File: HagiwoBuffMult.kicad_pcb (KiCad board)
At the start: 2 copper layers, 25 x 108.3 mm, 41 parts, among them J1 IN1, J10 Conn_01x01_Socket, J11 Conn_01x01_Socket, J12 Conn_01x01_Socket, J13 Conn_01x01_Socket, J14 Conn_01x01_Socket, J15 Conn_01x01_Socket, J16 Conn_01x01_Socket, J17 Conn_01x01_Socket, J18 Conn_01x01_Socket, J19 Conn_01x01_Socket, J2 IN2, J20 Conn_01x01_Pin, J21 Conn_01x01_Pin, J22 Conn_01x01_Pin, J23 Conn_01x01_Pin, J24 Conn_01x01_Pin, J25 Conn_01x01_Pin, J26 Conn_01x01_Pin, J27 Conn_01x01_Pin, J28 Conn_01x01_Pin, J29 Conn_01x01_Pin, J3 Eurorack_Power_10pin_Unshroud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, J4 OUT1, J5 OUT2, J6 OUT3, J7 OUT4, J8 OUT5, J9 OUT6, U1 TL074, U2 TL074

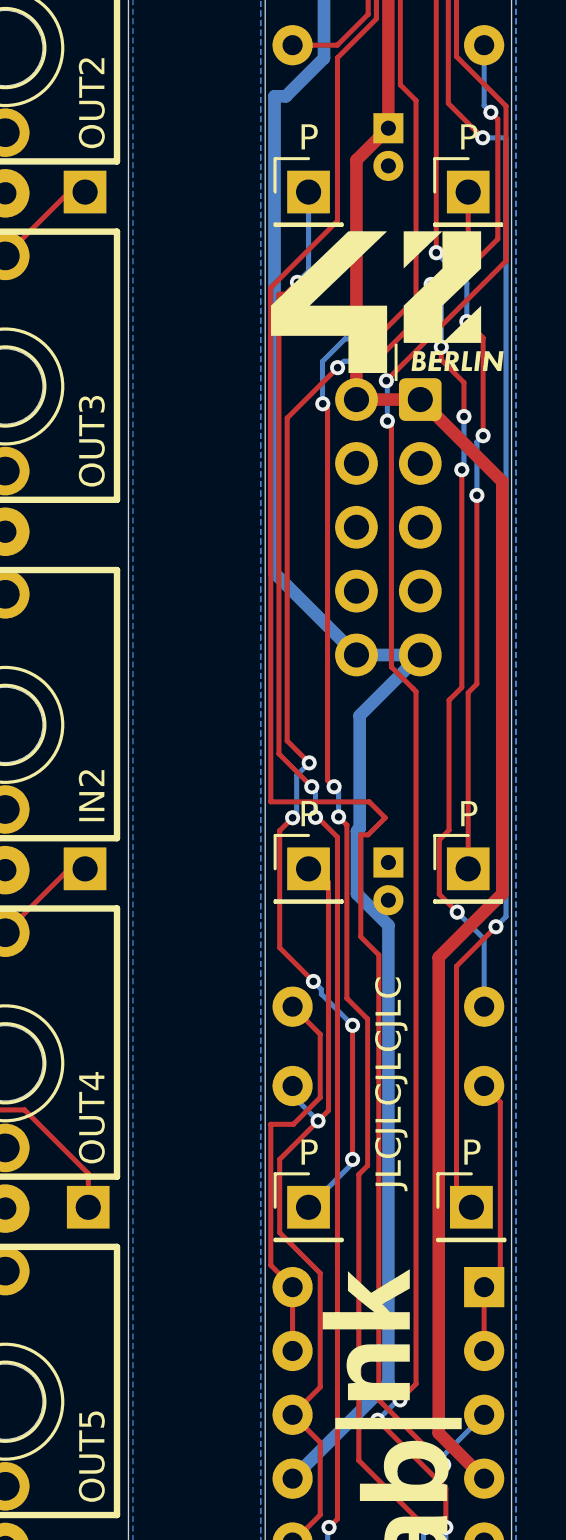
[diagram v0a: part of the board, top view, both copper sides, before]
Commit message: working on v1.1 - added build notes - widened 10uF cap footprint - what to do about traces being too close to board edge?
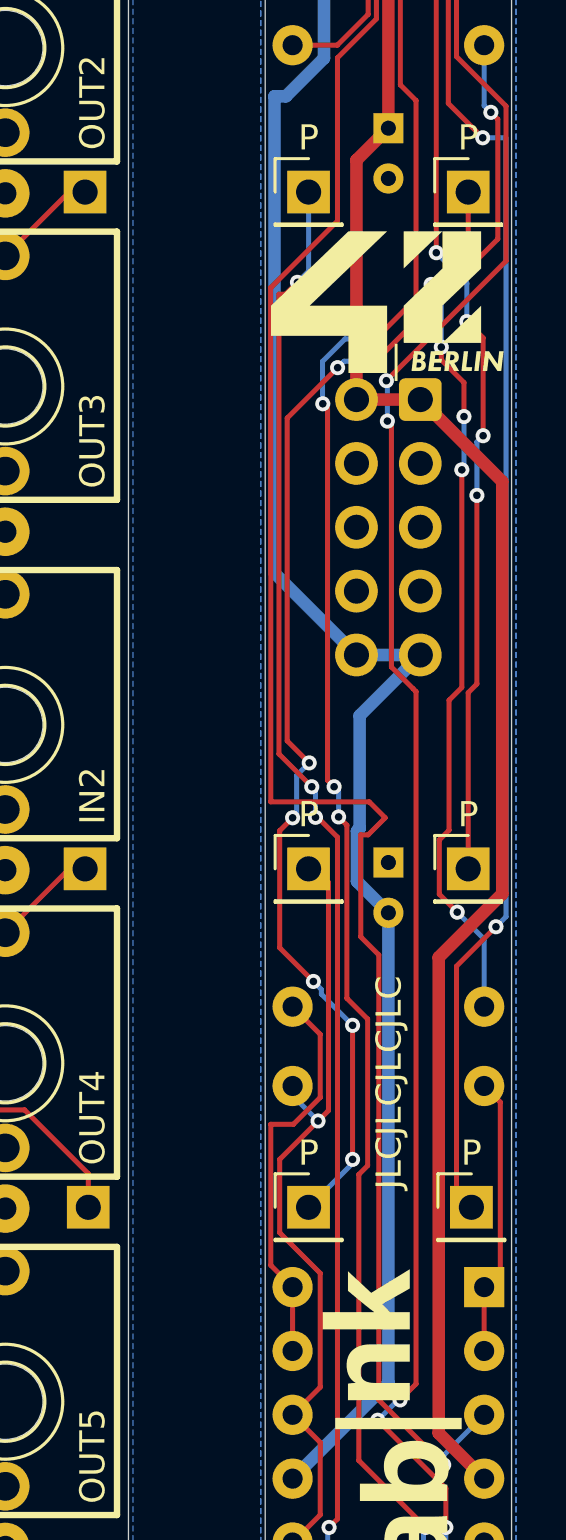
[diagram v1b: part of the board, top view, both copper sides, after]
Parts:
- C1, C2: footprint Capacitor_THT:CP_Radial_D4.0mm_P1.50mm -> Capacitor_THT:CP_Radial_D4.0mm_P2.00mm
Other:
- board text added: "V1.1"
- board text removed: "V1.0"

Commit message: v1.1 reaady for final check
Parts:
- added C3: 100nF, Capacitor_THT:C_Disc_D3.0mm_W1.6mm_P2.50mm, B.Cu at (72.5, 151.8)
- added C4: 100nF, Capacitor_THT:C_Disc_D3.0mm_W1.6mm_P2.50mm, B.Cu at (72.1, 55.5)
- added C5: 100nF, Capacitor_THT:C_Disc_D3.0mm_W1.6mm_P2.50mm, B.Cu at (69.5, 154.3)
- added C6: 100nF, Capacitor_THT:C_Disc_D3.0mm_W1.6mm_P2.50mm, B.Cu at (69.8, 53.0)
- R1, R2, R3, R4, R5, R6, R7, R8: footprint Resistor_THT:R_Axial_DIN0207_L6.3mm_D2.5mm_P7.62mm_Horizontal -> Resistor_THT:R_Axial_DIN0204_L3.6mm_D1.6mm_P1.90mm_Vertical
- moved R2 99.6 mm to (74.9, 151.9), turned to -90 degrees
- moved R8 96.6 mm to (67.3, 151.9), turned to -90 degrees
- moved U1 75.3 mm to (74.9, 58.4)
- moved U2 75.3 mm to (74.9, 133.7)
- moved R3 73.6 mm to (74.3, 81.5), turned to 90 degrees
- moved R1 70.3 mm to (74.9, 55.4), turned to 90 degrees
- moved R4 66.8 mm to (67.7, 85.3), turned to -90 degrees
- moved R7 41.4 mm to (67.9, 125.7), turned to -90 degrees
- moved R6 40.6 mm to (74.3, 121.9), turned to 90 degrees
- moved R5 37.9 mm to (74.5, 85.3), turned to -90 degrees
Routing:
- net OUT6_PIN1_C: track 111.4 -> 8.46 mm, vias 10 -> 0
- net OUT1_PIN1_C: track 86.2 -> 2.99 mm, vias 6 -> 0
- net IN2_PIN1_C: track 73.6 -> 9.08 mm, vias 4 -> 0
- net OUT2_PIN1_C: track 66.4 -> 3.23 mm, vias 7 -> 0
- net IN1_PIN1_C: track 75.6 -> 18.4 mm, vias 1 -> 2
- net OUT5_PIN1_C: track 53.4 -> 2.92 mm, vias 8 -> 0
- net IN2_PIN3_C: track 39.5 -> 87.0 mm, vias 1 -> 4
- net OUT4_PIN1_C: track 42.0 -> 2.92 mm, vias 6 -> 0
- net OUT3_PIN1_C: track 34.7 -> 3.05 mm, vias 5 -> 0
- net +12V: track 83.1 -> 107.4 mm
- net -12V: track 86.1 -> 108.5 mm
- net Net-(U2B-+): track 26.5 -> 47.5 mm
- net Net-(U1D--): track 15.9 -> 35.7 mm, vias 0 -> 3
- net Net-(U2B--): track 10.8 -> 28.5 mm, vias 0 -> 1
- net Net-(U1C--): track 5.71 -> 23.0 mm, vias 0 -> 2
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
